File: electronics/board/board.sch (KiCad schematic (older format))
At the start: 57 parts, among them J1 Conn_02x05_Odd_Even, J2 USB_A, J3 Micro_SD_Card_Det_Hirose_DM3AT, SW1 SW_Push, U1 JW5211, U2 JW5211, U3 JW5211, U4 F1C100s, U5 SST26VF080A-104I/SN, Y1 Crystal_GND24

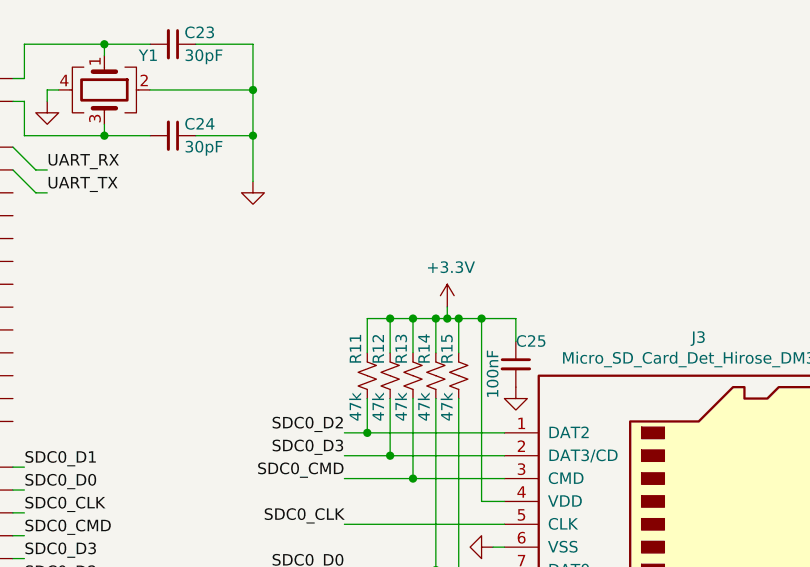
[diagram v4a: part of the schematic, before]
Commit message: Selected inductors.
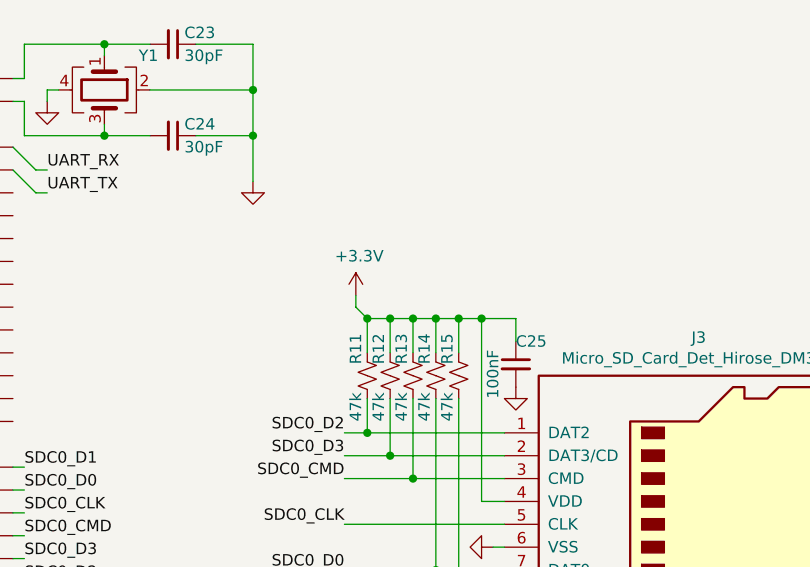
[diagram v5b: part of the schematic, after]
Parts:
- L1, L2, L3: footprint (none) -> Inductor_SMD:L_1008_2520Metric; MPN (none) -> CVH252009-1R5M
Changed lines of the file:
@@
 F 0 "L1" V 3635 2050 50  0000 C CNN
 F 1 "1.5uH" V 3544 2050 50  0000 C CNN
-F 2 "" H 3450 2050 50  0001 C CNN
+F 2 "Inductor_SMD:L_1008_2520Metric" H 3450 2050 50  0001 C CNN
 F 3 "~" H 3450 2050 50  0001 C CNN
+F 4 "CVH252009-1R5M" V 3450 2050 50  0001 C CNN "MPN"
 	1    3450 2050
 	0    -1   -1   0
@@
 F 0 "L2" V 3635 3250 50  0000 C CNN
 F 1 "1.5uH" V 3544 3250 50  0000 C CNN
-F 2 "" H 3450 3250 50  0001 C CNN
+F 2 "Inductor_SMD:L_1008_2520Metric" H 3450 3250 50  0001 C CNN
 F 3 "~" H 3450 3250 50  0001 C CNN
+F 4 "CVH252009-1R5M" V 3450 3250 50  0001 C CNN "MPN"
 	1    3450 3250
 	0    -1   -1   0
@@
 F 0 "L3" V 3635 4450 50  0000 C CNN
 F 1 "1.5uH" V 3544 4450 50  0000 C CNN
-F 2 "" H 3450 4450 50  0001 C CNN
+F 2 "Inductor_SMD:L_1008_2520Metric" H 3450 4450 50  0001 C CNN
 F 3 "~" H 3450 4450 50  0001 C CNN
+F 4 "CVH252009-1R5M" V 3450 4450 50  0001 C CNN "MPN"
 	1    3450 4450
 	0    -1   -1   0
@@
 L power:+3.3V #PWR039
 U 1 1 6115080F
-P 13100 2750
-F 0 "#PWR039" H 13100 2600 50  0001 C CNN
-F 1 "+3.3V" H 13115 2923 50  0000 C CNN
-F 2 "" H 13100 2750 50  0001 C CNN
-F 3 "" H 13100 2750 50  0001 C CNN
-	1    13100 2750
+P 12700 2700
+F 0 "#PWR039" H 12700 2550 50  0001 C CNN
+F 1 "+3.3V" H 12715 2873 50  0000 C CNN
+F 2 "" H 12700 2700 50  0001 C CNN
+F 3 "" H 12700 2700 50  0001 C CNN
+	1    12700 2700
 	1    0    0    -1
 $EndComp
@@
 Connection ~ 13050 2800
 Wire Wire Line
-	13050 2800 13100 2800
-Wire Wire Line
-	13100 2800 13100 2750
+	12700 2750 12700 2700
 Wire Wire Line
 	12750 3150 12750 3300
@@
 	13150 4000 13350 4000
 Wire Wire Line
-	13100 2800 13150 2800
-Wire Wire Line
 	13150 2800 13150 2950
-Connection ~ 13100 2800
 Wire Wire Line
 	13150 2800 13250 2800
@@
 Wire Wire Line
 	4250 4450 4350 4450
+Wire Wire Line
+	13050 2800 13150 2800
+Wire Wire Line
+	12750 2800 12700 2750
+Connection ~ 12750 2800
 $EndSCHEMATC

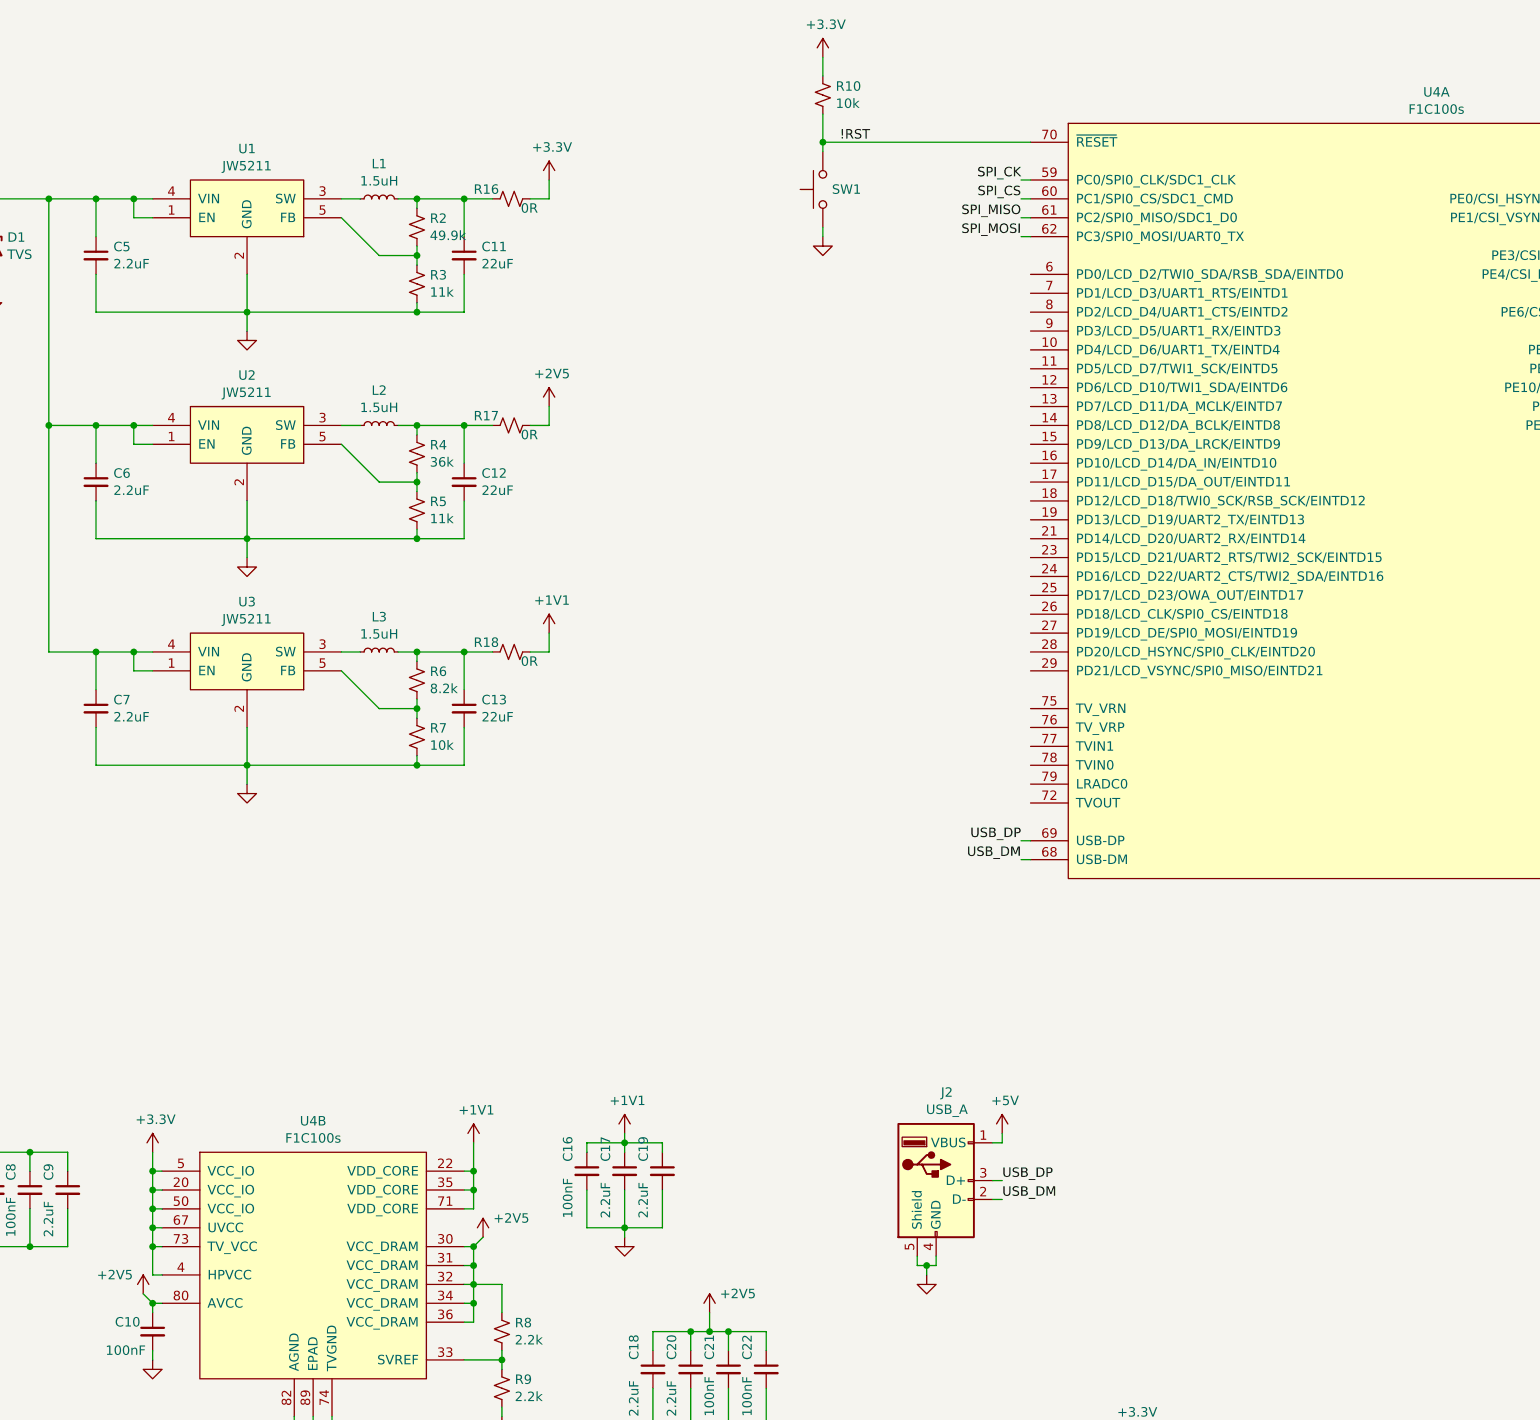
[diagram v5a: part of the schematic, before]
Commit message: Added USB power protection, started adding package footprints.
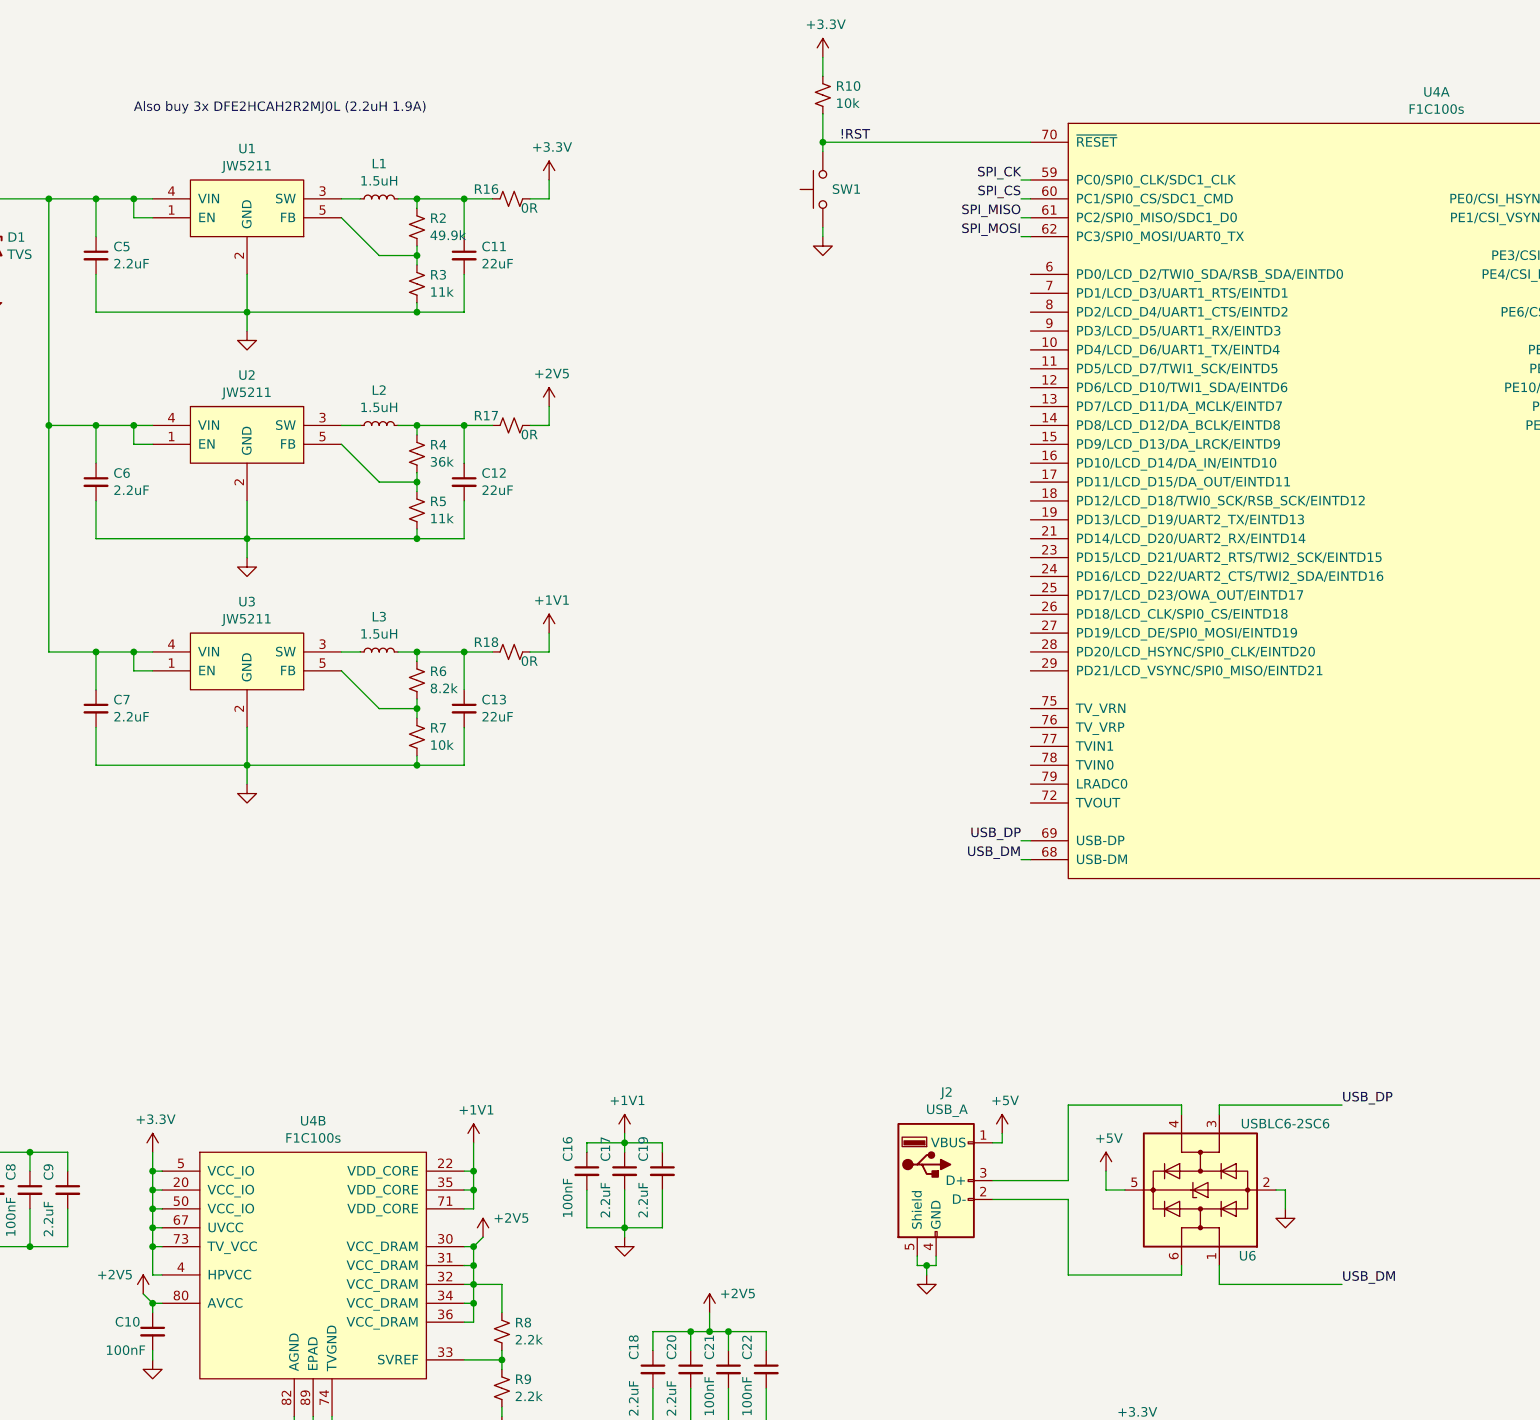
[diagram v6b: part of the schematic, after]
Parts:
- added U6: USBLC6-2SC6, Package_TO_SOT_SMD:SOT-23-6, symbol Power_Protection:USBLC6-2SC6
- C1, C10, C14, C15, C16, C17, C18, C19, C2, C20, C21, C22, C23, C24, C25, C3, C4, C5, C6, C7, C8, C9: footprint (none) -> Capacitor_SMD:C_0603_1608Metric
- C11, C12, C13: footprint (none) -> Capacitor_SMD:C_0805_2012Metric
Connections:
- net +5V: now also U6.5 (VBUS)
- net GND: now also U6.2 (GND)
- net USB_DM: now also U6.1 (I/O1); no longer J2.2 (D-)
- net USB_DP: now also U6.3 (I/O2); no longer J2.3 (D+)
- new net: J2.2 (D-), U6.6 (I/O1)
- new net: J2.3 (D+), U6.4 (I/O2)
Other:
- note added: "Also buy 3x DFE2HCAH2R2MJ0L (2.2uH 1.9A)"
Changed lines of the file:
@@
 F 0 "C5" H 2042 2396 50  0000 L CNN
 F 1 "2.2uF" H 2042 2305 50  0000 L CNN
-F 2 "" H 1950 2350 50  0001 C CNN
+F 2 "Capacitor_SMD:C_0603_1608Metric" H 1950 2350 50  0001 C CNN
 F 3 "~" H 1950 2350 50  0001 C CNN
 	1    1950 2350
@@
 F 0 "C11" H 3992 2396 50  0000 L CNN
 F 1 "22uF" H 3992 2305 50  0000 L CNN
-F 2 "" H 3900 2350 50  0001 C CNN
+F 2 "Capacitor_SMD:C_0805_2012Metric" H 3900 2350 50  0001 C CNN
 F 3 "~" H 3900 2350 50  0001 C CNN
 	1    3900 2350
@@
 F 0 "C10" H 2050 8100 50  0000 L CNN
 F 1 "100nF" H 2000 7950 50  0000 L CNN
-F 2 "" H 2250 8050 50  0001 C CNN
+F 2 "Capacitor_SMD:C_0603_1608Metric" H 2250 8050 50  0001 C CNN
 F 3 "~" H 2250 8050 50  0001 C CNN
 	1    2250 8050
@@
 F 0 "C1" V 700 7350 50  0000 L CNN
 F 1 "100nF" V 700 7050 50  0000 L CNN
-F 2 "" H 800 7300 50  0001 C CNN
+F 2 "Capacitor_SMD:C_0603_1608Metric" H 800 7300 50  0001 C CNN
 F 3 "~" H 800 7300 50  0001 C CNN
 	1    800  7300
@@
 F 0 "C2" V 900 7350 50  0000 L CNN
 F 1 "100nF" V 900 7050 50  0000 L CNN
-F 2 "" H 1000 7300 50  0001 C CNN
+F 2 "Capacitor_SMD:C_0603_1608Metric" H 1000 7300 50  0001 C CNN
 F 3 "~" H 1000 7300 50  0001 C CNN
 	1    1000 7300
@@
 F 0 "C3" V 1100 7350 50  0000 L CNN
 F 1 "100nF" V 1100 7050 50  0000 L CNN
-F 2 "" H 1200 7300 50  0001 C CNN
+F 2 "Capacitor_SMD:C_0603_1608Metric" H 1200 7300 50  0001 C CNN
 F 3 "~" H 1200 7300 50  0001 C CNN
 	1    1200 7300
@@
 F 0 "C4" V 1300 7350 50  0000 L CNN
 F 1 "100nF" V 1300 7050 50  0000 L CNN
-F 2 "" H 1400 7300 50  0001 C CNN
+F 2 "Capacitor_SMD:C_0603_1608Metric" H 1400 7300 50  0001 C CNN
 F 3 "~" H 1400 7300 50  0001 C CNN
 	1    1400 7300
@@
 F 0 "C8" V 1500 7350 50  0000 L CNN
 F 1 "100nF" V 1500 7050 50  0000 L CNN
-F 2 "" H 1600 7300 50  0001 C CNN
+F 2 "Capacitor_SMD:C_0603_1608Metric" H 1600 7300 50  0001 C CNN
 F 3 "~" H 1600 7300 50  0001 C CNN
 	1    1600 7300
@@
 F 0 "C9" V 1700 7350 50  0000 L CNN
 F 1 "2.2uF" V 1700 7050 50  0000 L CNN
-F 2 "" H 1800 7300 50  0001 C CNN
+F 2 "Capacitor_SMD:C_0603_1608Metric" H 1800 7300 50  0001 C CNN
 F 3 "~" H 1800 7300 50  0001 C CNN
 	1    1800 7300
@@
 F 0 "C16" V 4450 7250 50  0000 L CNN
 F 1 "100nF" V 4450 6950 50  0000 L CNN
-F 2 "" H 4550 7200 50  0001 C CNN
+F 2 "Capacitor_SMD:C_0603_1608Metric" H 4550 7200 50  0001 C CNN
 F 3 "~" H 4550 7200 50  0001 C CNN
 	1    4550 7200
@@
 F 0 "C17" V 4650 7250 50  0000 L CNN
 F 1 "2.2uF" V 4650 6950 50  0000 L CNN
-F 2 "" H 4750 7200 50  0001 C CNN
+F 2 "Capacitor_SMD:C_0603_1608Metric" H 4750 7200 50  0001 C CNN
 F 3 "~" H 4750 7200 50  0001 C CNN
 	1    4750 7200
@@
 F 0 "C19" V 4850 7250 50  0000 L CNN
 F 1 "2.2uF" V 4850 6950 50  0000 L CNN
-F 2 "" H 4950 7200 50  0001 C CNN
+F 2 "Capacitor_SMD:C_0603_1608Metric" H 4950 7200 50  0001 C CNN
 F 3 "~" H 4950 7200 50  0001 C CNN
 	1    4950 7200
@@
 F 0 "C18" V 4800 8300 50  0000 L CNN
 F 1 "2.2uF" V 4800 8000 50  0000 L CNN
-F 2 "" H 4900 8250 50  0001 C CNN
+F 2 "Capacitor_SMD:C_0603_1608Metric" H 4900 8250 50  0001 C CNN
 F 3 "~" H 4900 8250 50  0001 C CNN
 	1    4900 8250
@@
 F 0 "C20" V 5000 8300 50  0000 L CNN
 F 1 "2.2uF" V 5000 8000 50  0000 L CNN
-F 2 "" H 5100 8250 50  0001 C CNN
+F 2 "Capacitor_SMD:C_0603_1608Metric" H 5100 8250 50  0001 C CNN
 F 3 "~" H 5100 8250 50  0001 C CNN
 	1    5100 8250
@@
 F 0 "C21" V 5200 8300 50  0000 L CNN
 F 1 "100nF" V 5200 8000 50  0000 L CNN
-F 2 "" H 5300 8250 50  0001 C CNN
+F 2 "Capacitor_SMD:C_0603_1608Metric" H 5300 8250 50  0001 C CNN
 F 3 "~" H 5300 8250 50  0001 C CNN
 	1    5300 8250
@@
 F 0 "C22" V 5400 8300 50  0000 L CNN
 F 1 "100nF" V 5400 8000 50  0000 L CNN
-F 2 "" H 5500 8250 50  0001 C CNN
+F 2 "Capacitor_SMD:C_0603_1608Metric" H 5500 8250 50  0001 C CNN
 F 3 "~" H 5500 8250 50  0001 C CNN
 	1    5500 8250
@@
 F 0 "C6" H 2042 3596 50  0000 L CNN
 F 1 "2.2uF" H 2042 3505 50  0000 L CNN
-F 2 "" H 1950 3550 50  0001 C CNN
+F 2 "Capacitor_SMD:C_0603_1608Metric" H 1950 3550 50  0001 C CNN
 F 3 "~" H 1950 3550 50  0001 C CNN
 	1    1950 3550
@@
 F 0 "C12" H 3992 3596 50  0000 L CNN
 F 1 "22uF" H 3992 3505 50  0000 L CNN
-F 2 "" H 3900 3550 50  0001 C CNN
+F 2 "Capacitor_SMD:C_0805_2012Metric" H 3900 3550 50  0001 C CNN
 F 3 "~" H 3900 3550 50  0001 C CNN
 	1    3900 3550
@@
 F 0 "C7" H 2042 4796 50  0000 L CNN
 F 1 "2.2uF" H 2042 4705 50  0000 L CNN
-F 2 "" H 1950 4750 50  0001 C CNN
+F 2 "Capacitor_SMD:C_0603_1608Metric" H 1950 4750 50  0001 C CNN
 F 3 "~" H 1950 4750 50  0001 C CNN
 	1    1950 4750
@@
 F 0 "C13" H 3992 4796 50  0000 L CNN
 F 1 "22uF" H 3992 4705 50  0000 L CNN
-F 2 "" H 3900 4750 50  0001 C CNN
+F 2 "Capacitor_SMD:C_0805_2012Metric" H 3900 4750 50  0001 C CNN
 F 3 "~" H 3900 4750 50  0001 C CNN
 	1    3900 4750
@@
 F 0 "C14" H 7200 9000 50  0000 L CNN
 F 1 "100nF" H 7250 8800 50  0000 R CNN
-F 2 "" H 7300 8900 50  0001 C CNN
+F 2 "Capacitor_SMD:C_0603_1608Metric" H 7300 8900 50  0001 C CNN
 F 3 "~" H 7300 8900 50  0001 C CNN
 	1    7300 8900
@@
 F 0 "C15" H 7700 9000 50  0000 R CNN
 F 1 "100nF" H 7650 8800 50  0000 L CNN
-F 2 "" H 7600 8900 50  0001 C CNN
+F 2 "Capacitor_SMD:C_0603_1608Metric" H 7600 8900 50  0001 C CNN
 F 3 "~" H 7600 8900 50  0001 C CNN
 	1    7600 8900
@@
 Text Label 6850 5550 2    50   ~ 0
 USB_DM
-Text Label 6750 7250 0    50   ~ 0
+Text Label 8550 6850 0    50   ~ 0
 USB_DP
-Text Label 6750 7350 0    50   ~ 0
+Text Label 8550 7800 0    50   ~ 0
 USB_DM
 $Comp
@@
 Wire Wire Line
 	6750 7050 6700 7050
-Wire Wire Line
-	6750 7250 6700 7250
-Wire Wire Line
-	6750 7350 6700 7350
 Wire Wire Line
 	6300 7650 6300 7700
@@
 F 0 "C23" V 11850 1650 50  0000 L CNN
 F 1 "30pF" V 11950 1650 50  0000 L CNN
-F 2 "" H 11900 1600 50  0001 C CNN
+F 2 "Capacitor_SMD:C_0603_1608Metric" H 11900 1600 50  0001 C CNN
 F 3 "~" H 11900 1600 50  0001 C CNN
 	1    11900 1600
@@
 F 0 "C24" V 11850 2050 50  0000 L CNN
 F 1 "30pF" V 11950 2050 50  0000 L CNN
-F 2 "" H 11900 2000 50  0001 C CNN
+F 2 "Capacitor_SMD:C_0603_1608Metric" H 11900 2000 50  0001 C CNN
 F 3 "~" H 11900 2000 50  0001 C CNN
 	1    11900 2000
@@
 F 0 "C25" H 13400 3100 50  0000 L CNN
 F 1 "100nF" V 13300 2850 50  0000 L CNN
-F 2 "" H 13400 3000 50  0001 C CNN
+F 2 "Capacitor_SMD:C_0603_1608Metric" H 13400 3000 50  0001 C CNN
 F 3 "~" H 13400 3000 50  0001 C CNN
 	1    13400 3000
@@
 	12750 2800 12700 2750
 Connection ~ 12750 2800
+Text Notes 2150 1600 0    50   ~ 0
+Also buy 3x DFE2HCAH2R2MJ0L (2.2uH 1.9A)
+Wire Wire Line
+	7100 7350 6700 7350
+Wire Wire Line
+	6700 7250 7100 7250
+Wire Wire Line
+	7100 7350 7100 7750
+Wire Wire Line
+	7100 7750 7700 7750
+Wire Wire Line
+	7700 7750 7700 7700
+$Comp
+L Power_Protection:USBLC6-2SC6 U6
+U 1 1 615D8B8D
+P 7800 7300
+F 0 "U6" V 7450 7050 50  0000 C CNN
+F 1 "USBLC6-2SC6" V 8150 6850 50  0000 C CNN
+F 2 "Package_TO_SOT_SMD:SOT-23-6" H 7800 6800 50  0001 C CNN
+F 3 "https://www.st.com/resource/en/datasheet/usblc6-2.pdf" H 8000 7650 50  0001 C CNN
+	1    7800 7300
+	0    -1   -1   0
+$EndComp
+Wire Wire Line
+	7100 6850 7700 6850
+Wire Wire Line
+	7100 6850 7100 7250
+Wire Wire Line
+	7700 6850 7700 6900
+Wire Wire Line
+	7400 7300 7300 7300
+Wire Wire Line
+	7300 7300 7300 7200
+$Comp
+L power:+5V #PWR042
+U 1 1 616E610E
+P 7300 7200
+F 0 "#PWR042" H 7300 7050 50  0001 C CNN
+F 1 "+5V" H 7315 7373 50  0000 C CNN
+F 2 "" H 7300 7200 50  0001 C CNN
+F 3 "" H 7300 7200 50  0001 C CNN
+	1    7300 7200
+	1    0    0    -1
+$EndComp
+Wire Wire Line
+	7900 7700 7900 7800
+Wire Wire Line
+	7900 7800 8550 7800
+Wire Wire Line
+	7900 6900 7900 6850
+Wire Wire Line
+	7900 6850 8550 6850
+Wire Wire Line
+	8200 7300 8250 7300
+Wire Wire Line
+	8250 7300 8250 7400
+$Comp
+L power:GND #PWR043
+U 1 1 6172E5C7
+P 8250 7400
+F 0 "#PWR043" H 8250 7150 50  0001 C CNN
+F 1 "GND" H 8255 7227 50  0001 C CNN
+F 2 "" H 8250 7400 50  0001 C CNN
+F 3 "" H 8250 7400 50  0001 C CNN
+	1    8250 7400
+	1    0    0    -1
+$EndComp
 $EndSCHEMATC
